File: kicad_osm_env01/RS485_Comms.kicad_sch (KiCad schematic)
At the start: 15 parts

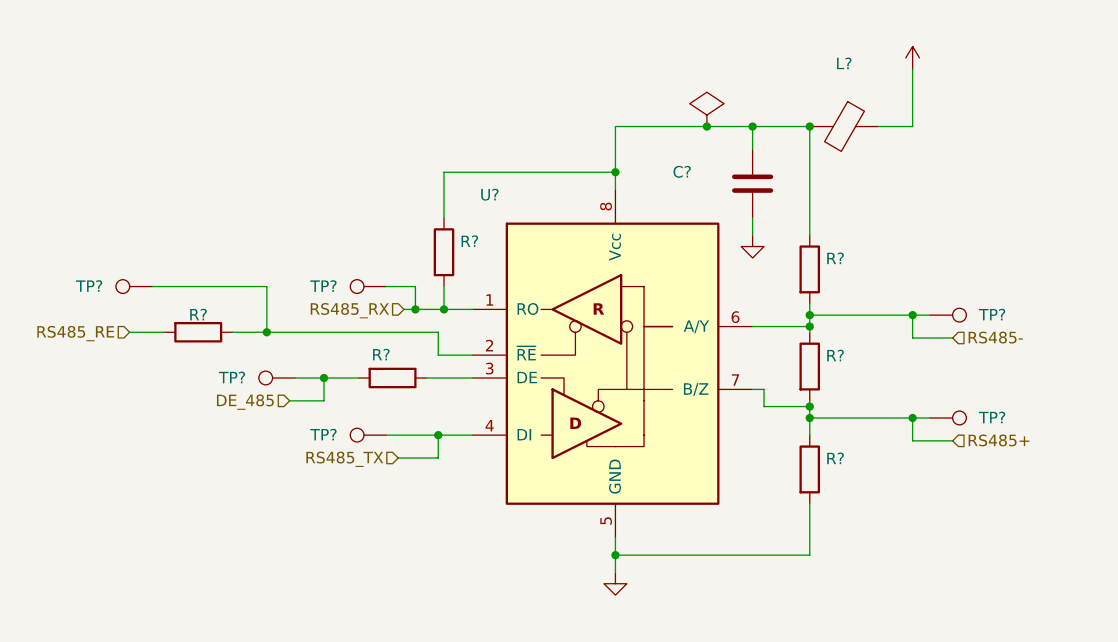
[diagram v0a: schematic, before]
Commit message: added stml433 to schematic and carried out some mods
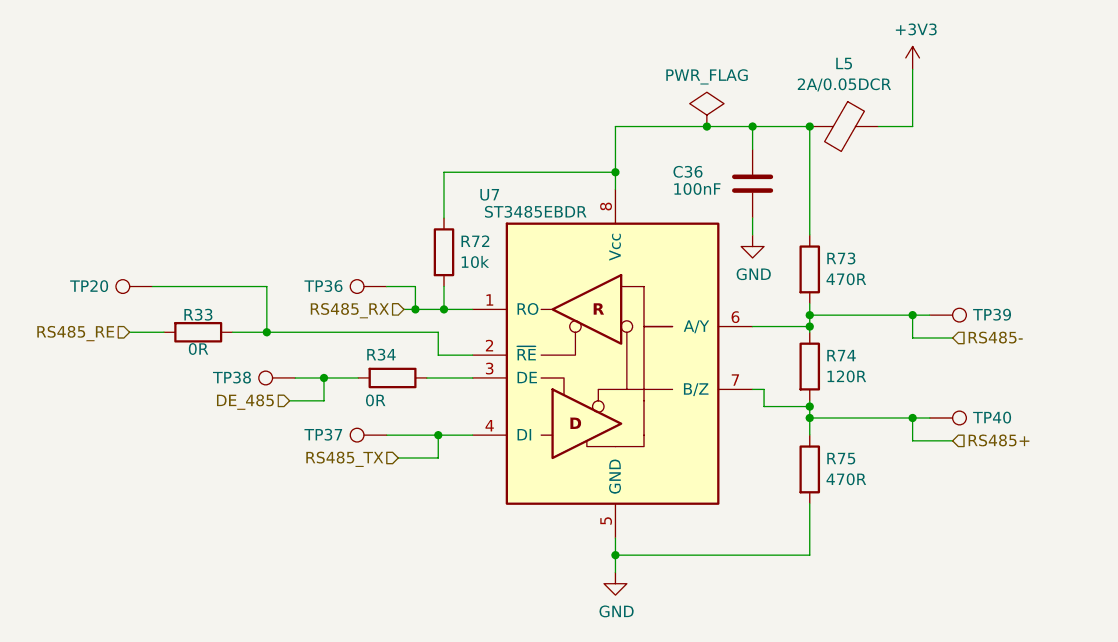
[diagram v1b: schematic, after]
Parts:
- C36: renamed from C?; value (none) -> 100nF; footprint (none) -> Capacitor_SMD:C_0402_1005Metric
- L5: renamed from L?; value (none) -> 2A/0.05DCR; footprint (none) -> Inductor_SMD:L_0402_1005Metric
- R33, R34: renamed from R?; value (none) -> 0R; footprint (none) -> Resistor_SMD:R_0603_1608Metric
- R72: renamed from R?; value (none) -> 10k; footprint (none) -> Resistor_SMD:R_0603_1608Metric
- R73, R75: renamed from R?; value (none) -> 470R; footprint (none) -> Resistor_SMD:R_0603_1608Metric
- R74: renamed from R?; value (none) -> 120R; footprint (none) -> Resistor_SMD:R_0603_1608Metric
- TP20, TP36, TP37, TP38, TP39, TP40: renamed from TP?; value (none) -> Test_Point; footprint (none) -> TestPoint:TestPoint_Pad_D1.5mm
- U7: renamed from U?; value (none) -> ST3485EBDR; footprint (none) -> Package_SO:SOIC-8_3.9x4.9mm_P1.27mm

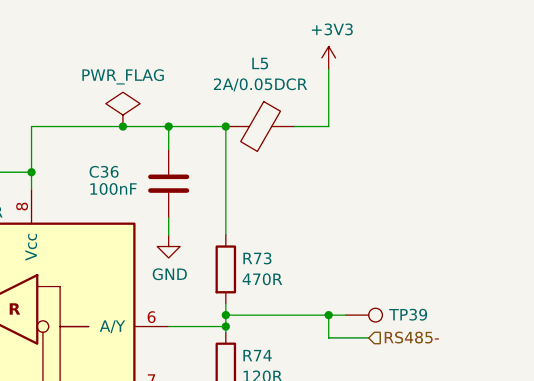
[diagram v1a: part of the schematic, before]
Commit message: updated schematics
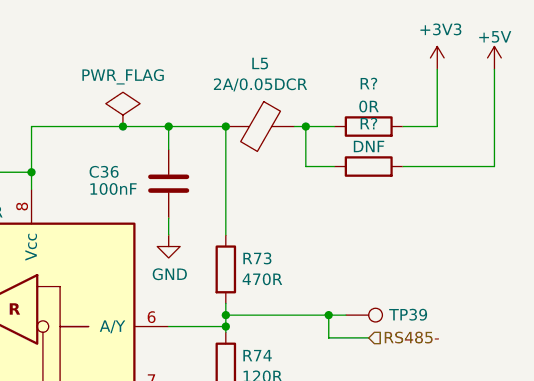
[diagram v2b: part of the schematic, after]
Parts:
- added R?: DNF, symbol device:R
- added R?: 0R, symbol device:R
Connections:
- net +3V3: now also R?.2; no longer L5.1
- new net: L5.1, R?.1, R?.1
- new net +5V: R?.2
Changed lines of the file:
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@@
     (comment 1 "Part No: 304-010")
   )
+  (junction (at 173.99 71.755) (diameter 0) (color 0 0 0 0)
+  )
   (junction (at 176.53 104.14) (diameter 0) (color 0 0 0 0)
   )
@@
   (junction (at 124.46 92.075) (diameter 0) (color 0 0 0 0)
   )
+  (wire (pts (xy 172.72 71.755) (xy 173.99 71.755))
+    (stroke (width 0) (type default) (color 0 0 0 0))
+  )
   (wire (pts (xy 158.75 83.82) (xy 158.75 81.915))
     (stroke (width 0) (type default) (color 0 0 0 0))
@@
     (stroke (width 0) (type default) (color 0 0 0 0))
   )
+  (wire (pts (xy 184.785 76.2) (xy 194.945 76.2))
+    (stroke (width 0) (type default) (color 0 0 0 0))
+  )
   (wire (pts (xy 165.1 104.14) (xy 176.53 104.14))
     (stroke (width 0) (type default) (color 0 0 0 0))
@@
     (stroke (width 0) (type default) (color 0 0 0 0))
   )
-  (wire (pts (xy 172.72 71.755) (xy 176.53 71.755))
+  (wire (pts (xy 184.785 71.755) (xy 188.595 71.755))
     (stroke (width 0) (type default) (color 0 0 0 0))
   )
@@
     (stroke (width 0) (type default) (color 0 0 0 0))
   )
+  (wire (pts (xy 173.99 71.755) (xy 177.165 71.755))
+    (stroke (width 0) (type default) (color 0 0 0 0))
+  )
+  (wire (pts (xy 194.945 65.405) (xy 194.945 76.2))
+    (stroke (width 0) (type default) (color 0 0 0 0))
+  )
   (wire (pts (xy 121.285 89.535) (xy 121.285 92.075))
     (stroke (width 0) (type default) (color 0 0 0 0))
@@
     (stroke (width 0) (type default) (color 0 0 0 0))
   )
+  (wire (pts (xy 177.165 76.2) (xy 173.99 76.2))
+    (stroke (width 0) (type default) (color 0 0 0 0))
+  )
   (wire (pts (xy 123.825 106.045) (xy 127.635 106.045))
     (stroke (width 0) (type default) (color 0 0 0 0))
@@
     (stroke (width 0) (type default) (color 0 0 0 0))
   )
-  (wire (pts (xy 176.53 65.405) (xy 176.53 71.755))
+  (wire (pts (xy 188.595 65.405) (xy 188.595 71.755))
     (stroke (width 0) (type default) (color 0 0 0 0))
   )
@@
   )
   (wire (pts (xy 165.1 71.755) (xy 165.1 83.82))
+    (stroke (width 0) (type default) (color 0 0 0 0))
+  )
+  (wire (pts (xy 173.99 76.2) (xy 173.99 71.755))
     (stroke (width 0) (type default) (color 0 0 0 0))
   )
@@
     (pin "2")
   )
-  (symbol (lib_id "power:+3V3") (at 176.53 65.405 0) (unit 1)
-    (in_bom yes) (on_board yes)
-    (property "Reference" "#PWR0150" (id 0) (at 176.53 69.215 0)
-      (effects (font (size 1.27 1.27)) hide)
-    )
-    (property "Value" "+3V3" (id 1) (at 176.911 61.0108 0))
-    (property "Footprint" "" (id 2) (at 176.53 65.405 0)
-      (effects (font (size 1.27 1.27)) hide)
-    )
-    (property "Datasheet" "" (id 3) (at 176.53 65.405 0)
+  (symbol (lib_id "power:+3V3") (at 188.595 65.405 0) (unit 1)
+    (in_bom yes) (on_board yes)
+    (property "Reference" "#PWR0150" (id 0) (at 188.595 69.215 0)
+      (effects (font (size 1.27 1.27)) hide)
+    )
+    (property "Value" "+3V3" (id 1) (at 188.976 61.0108 0))
+    (property "Footprint" "" (id 2) (at 188.595 65.405 0)
+      (effects (font (size 1.27 1.27)) hide)
+    )
+    (property "Datasheet" "" (id 3) (at 188.595 65.405 0)
       (effects (font (size 1.27 1.27)) hide)
     )
@@
     )
     (pin "1")
+  )
+  (symbol (lib_id "device:R") (at 180.975 76.2 90) (unit 1)
+    (in_bom yes) (on_board yes) (fields_autoplaced)
+    (property "Reference" "R?" (id 0) (at 180.975 71.4842 90))
+    (property "Value" "DNF" (id 1) (at 180.975 74.0211 90))
+    (property "Footprint" "" (id 2) (at 180.975 77.978 90)
+      (effects (font (size 1.27 1.27)) hide)
+    )
+    (property "Datasheet" "" (id 3) (at 180.975 76.2 0)
+      (effects (font (size 1.27 1.27)) hide)
+    )
+    (pin "1")
+    (pin "2")
+  )
+  (symbol (lib_id "device:R") (at 180.975 71.755 90) (unit 1)
+    (in_bom yes) (on_board yes) (fields_autoplaced)
+    (property "Reference" "R?" (id 0) (at 180.975 67.0392 90))
+    (property "Value" "0R" (id 1) (at 180.975 69.5761 90))
+    (property "Footprint" "" (id 2) (at 180.975 73.533 90)
+      (effects (font (size 1.27 1.27)) hide)
+    )
+    (property "Datasheet" "" (id 3) (at 180.975 71.755 0)
+      (effects (font (size 1.27 1.27)) hide)
+    )
+    (pin "1")
+    (pin "2")
+  )
+  (symbol (lib_id "OSM_env01:+5V") (at 194.945 65.405 0) (unit 1)
+    (in_bom yes) (on_board yes) (fields_autoplaced)
+    (property "Reference" "#PWR?" (id 0) (at 194.945 69.215 0)
+      (effects (font (size 1.27 1.27)) hide)
+    )
+    (property "Value" "+5V" (id 1) (at 194.945 61.8292 0))
+    (property "Footprint" "" (id 2) (at 194.945 65.405 0)
+      (effects (font (size 1.524 1.524)))
+    )
+    (property "Datasheet" "" (id 3) (at 194.945 65.405 0)
+      (effects (font (size 1.524 1.524)))
+    )
+    (pin "1")

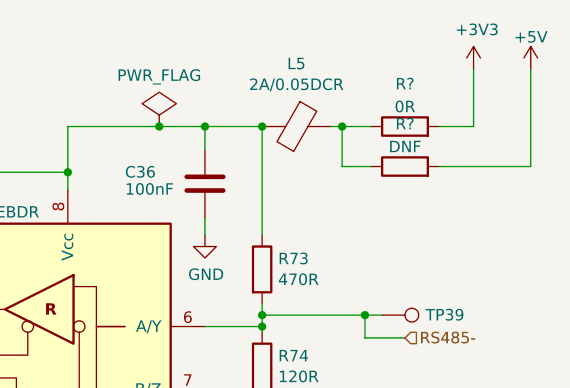
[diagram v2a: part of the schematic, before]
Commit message: added new battery charge ic u2
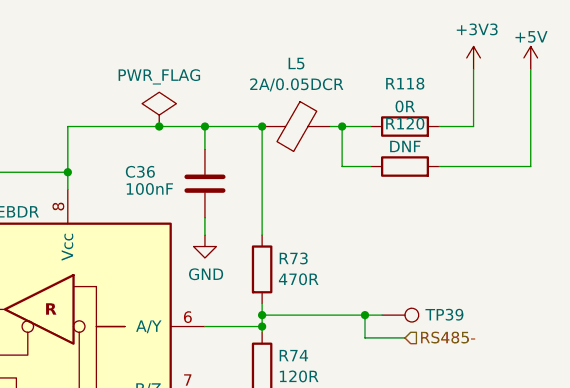
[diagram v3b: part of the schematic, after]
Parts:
- gave numbers to parts that had none: 2
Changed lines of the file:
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@@
   (title_block
     (title "Open Smart Monitor")
-    (date "2021-09-29")
-    (rev "B")
+    (date "2022-07-01")
+    (rev "C")
     (company "Devtank LTD")
     (comment 1 "Part No: 304-010")
@@
   (symbol (lib_id "device:R") (at 180.975 76.2 90) (unit 1)
     (in_bom yes) (on_board yes) (fields_autoplaced)
-    (property "Reference" "R?" (id 0) (at 180.975 71.4842 90))
+    (property "Reference" "R120" (id 0) (at 180.975 71.4842 90))
     (property "Value" "DNF" (id 1) (at 180.975 74.0211 90))
     (property "Footprint" "" (id 2) (at 180.975 77.978 90)
@@
   (symbol (lib_id "device:R") (at 180.975 71.755 90) (unit 1)
     (in_bom yes) (on_board yes) (fields_autoplaced)
-    (property "Reference" "R?" (id 0) (at 180.975 67.0392 90))
+    (property "Reference" "R118" (id 0) (at 180.975 67.0392 90))
     (property "Value" "0R" (id 1) (at 180.975 69.5761 90))
     (property "Footprint" "" (id 2) (at 180.975 73.533 90)
@@
   (symbol (lib_id "OSM_env01:+5V") (at 194.945 65.405 0) (unit 1)
     (in_bom yes) (on_board yes) (fields_autoplaced)
-    (property "Reference" "#PWR?" (id 0) (at 194.945 69.215 0)
-      (effects (font (size 1.27 1.27)) hide)
-    )
+    (property "Reference" "#PWR096" (id 0) (at 194.945 69.215 0)
+      (effects (font (size 1.27 1.27)) hide)
+    )

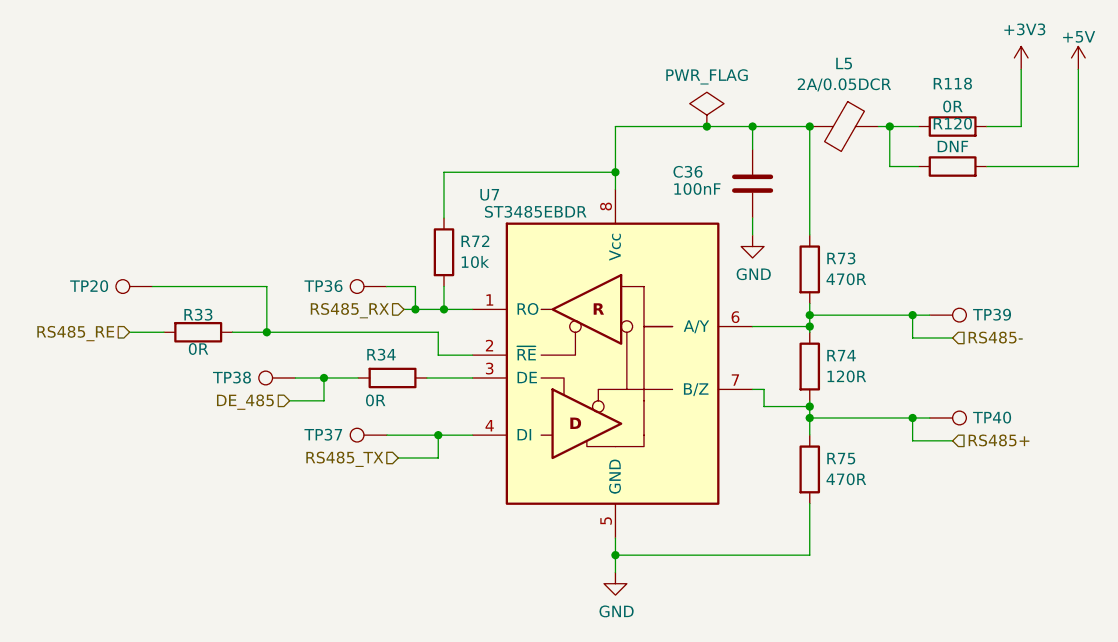
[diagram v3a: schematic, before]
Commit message: Schematics waiting review
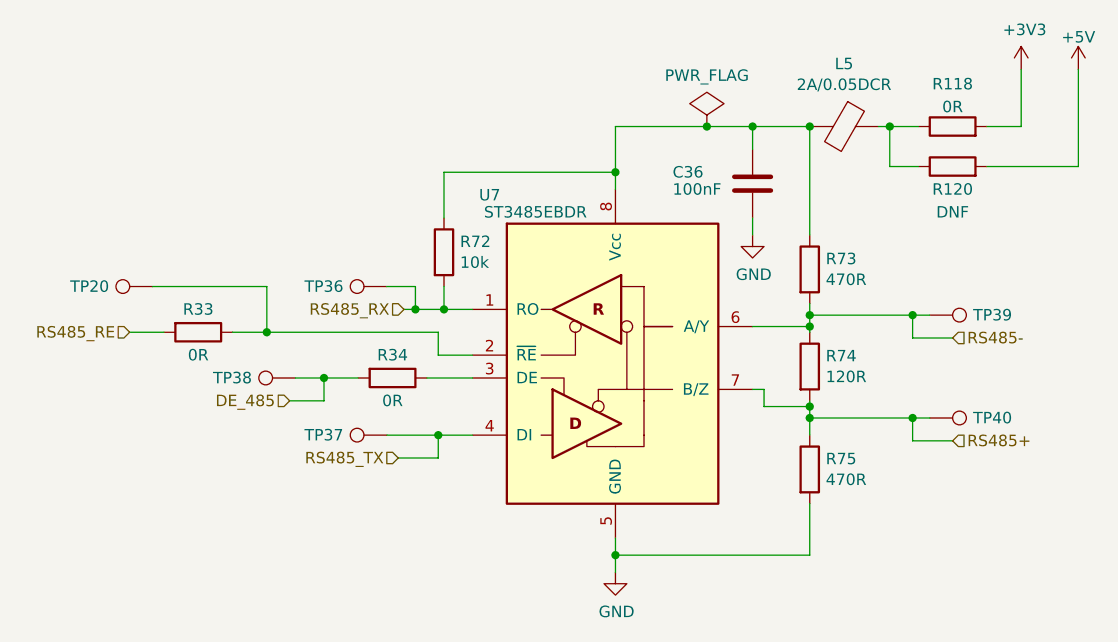
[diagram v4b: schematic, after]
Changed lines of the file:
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@@
   (symbol (lib_id "device:R") (at 118.745 99.695 270) (unit 1)
     (in_bom yes) (on_board yes)
-    (property "Reference" "R34" (id 0) (at 117.475 97.155 90))
-    (property "Value" "0R" (id 1) (at 116.84 102.235 90))
+    (property "Reference" "R34" (id 0) (at 118.745 97.155 90))
+    (property "Value" "0R" (id 1) (at 118.745 102.235 90))
     (property "Footprint" "Resistor_SMD:R_0603_1608Metric" (id 2) (at 118.745 97.917 90)
       (effects (font (size 1.27 1.27)) hide)
@@
   (symbol (lib_id "device:R") (at 97.155 94.615 270) (unit 1)
     (in_bom yes) (on_board yes)
-    (property "Reference" "R33" (id 0) (at 97.155 92.71 90))
-    (property "Value" "0R" (id 1) (at 97.155 96.52 90))
+    (property "Reference" "R33" (id 0) (at 97.155 92.075 90))
+    (property "Value" "0R" (id 1) (at 97.155 97.155 90))
     (property "Footprint" "Resistor_SMD:R_0603_1608Metric" (id 2) (at 97.155 92.837 90)
       (effects (font (size 1.27 1.27)) hide)
@@
   )
   (symbol (lib_id "device:R") (at 180.975 76.2 90) (unit 1)
-    (in_bom yes) (on_board yes) (fields_autoplaced)
-    (property "Reference" "R120" (id 0) (at 180.975 71.4842 90))
-    (property "Value" "DNF" (id 1) (at 180.975 74.0211 90))
+    (in_bom yes) (on_board yes)
+    (property "Reference" "R120" (id 0) (at 180.975 78.74 90))
+    (property "Value" "DNF" (id 1) (at 180.975 81.28 90))
     (property "Footprint" "" (id 2) (at 180.975 77.978 90)
       (effects (font (size 1.27 1.27)) hide)

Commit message: started layout with throwdown
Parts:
- C36: value 100nF -> (none); footprint Capacitor_SMD:C_0402_1005Metric -> (none); symbol OSM_env01-rescue:C-device-ESP32-EVB_Rev_D-rescue -> Device:C
- L5: value 2A/0.05DCR -> (none); footprint Inductor_SMD:L_0402_1005Metric -> (none); symbol device:Ferrite_Bead -> Device:FerriteBead
- R118: value 0R -> (none); symbol device:R -> Device:R
- R120: value DNF -> (none); symbol device:R -> Device:R
- R33, R34: value 0R -> (none); footprint Resistor_SMD:R_0603_1608Metric -> (none); symbol device:R -> Device:R
- R72: value 10k -> (none); footprint Resistor_SMD:R_0603_1608Metric -> (none); symbol OSM_env01-rescue:R-device-ESP32-EVB_Rev_D-rescue -> Device:R
- R73, R75: value 470R -> (none); footprint Resistor_SMD:R_0603_1608Metric -> (none); symbol OSM_env01-rescue:R-device-ESP32-EVB_Rev_D-rescue -> Device:R
- R74: value 120R -> (none); footprint Resistor_SMD:R_0603_1608Metric -> (none); symbol OSM_env01-rescue:R-device-ESP32-EVB_Rev_D-rescue -> Device:R
- TP20, TP36, TP37, TP38, TP39, TP40: value Test_Point -> (none); footprint TestPoint:TestPoint_Pad_D1.5mm -> (none)
- U7: value ST3485EBDR -> (none); footprint Package_SO:SOIC-8_3.9x4.9mm_P1.27mm -> (none)
